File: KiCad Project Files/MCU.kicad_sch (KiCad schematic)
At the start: 25 parts, among them SW1 Boot, SW2 Reset, U1 RP2040, U2 W25Q128JVS, Y1 12MHz

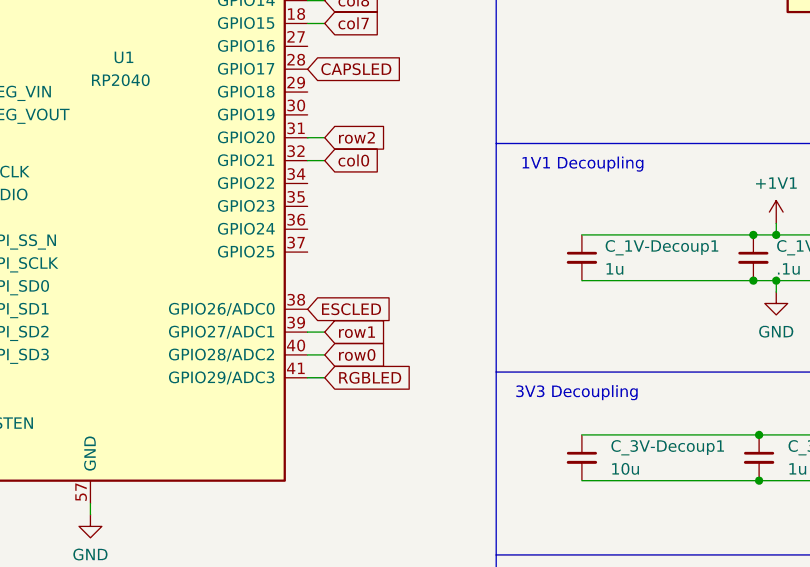
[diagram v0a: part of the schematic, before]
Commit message: Add files via upload
updated schematics
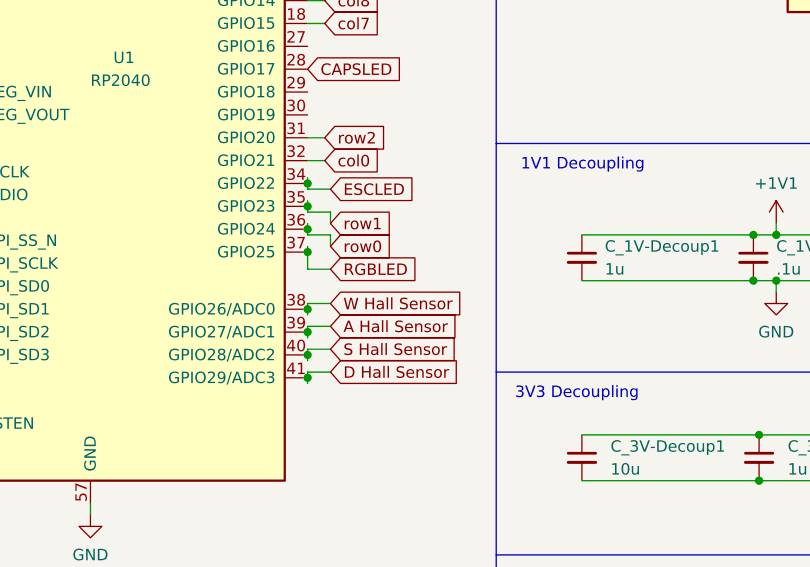
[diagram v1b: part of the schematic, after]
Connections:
- net ESCLED: now also U1.34 (GPIO22); no longer U1.38 (GPIO26/ADC0)
- net RGBLED: now also U1.37 (GPIO25); no longer U1.41 (GPIO29/ADC3)
- net row0: now also U1.36 (GPIO24); no longer U1.40 (GPIO28/ADC2)
- net row1: now also U1.35 (GPIO23); no longer U1.39 (GPIO27/ADC1)
- new net A Hall Sensor: U1.39 (GPIO27/ADC1)
- new net D Hall Sensor: U1.41 (GPIO29/ADC3)
- new net S Hall Sensor: U1.40 (GPIO28/ADC2)
- new net W Hall Sensor: U1.38 (GPIO26/ADC0)
